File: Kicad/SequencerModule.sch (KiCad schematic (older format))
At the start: 13 parts, among them U1 L78L05_SOT89, U2 MCP4822, U4 TL072

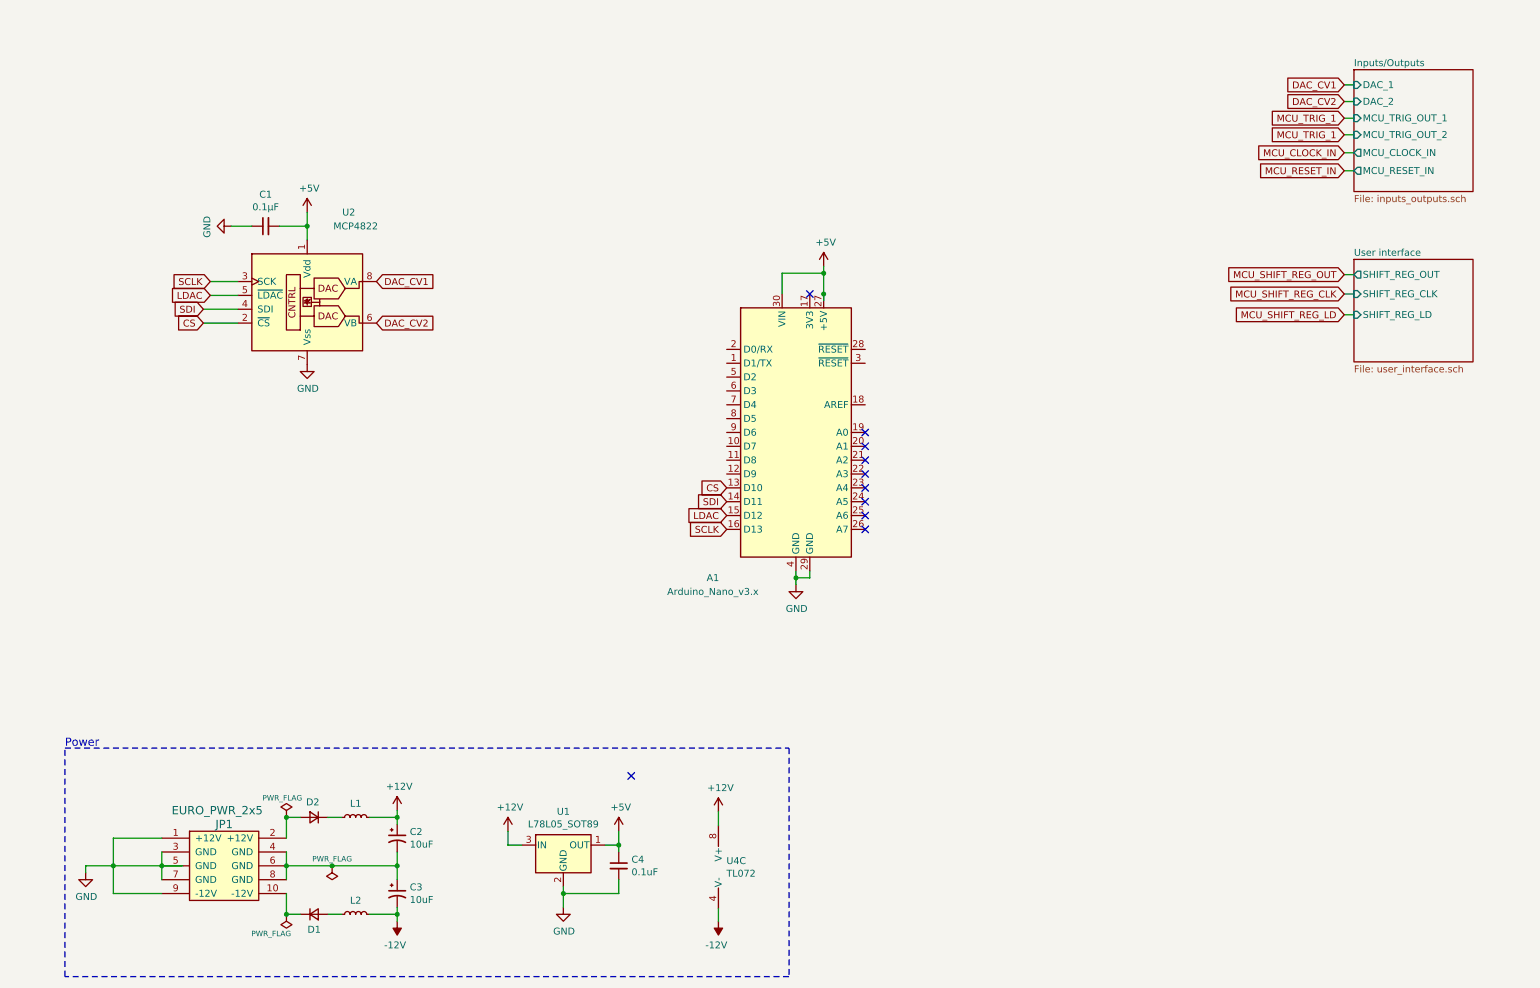
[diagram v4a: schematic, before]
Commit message: correcting some connections
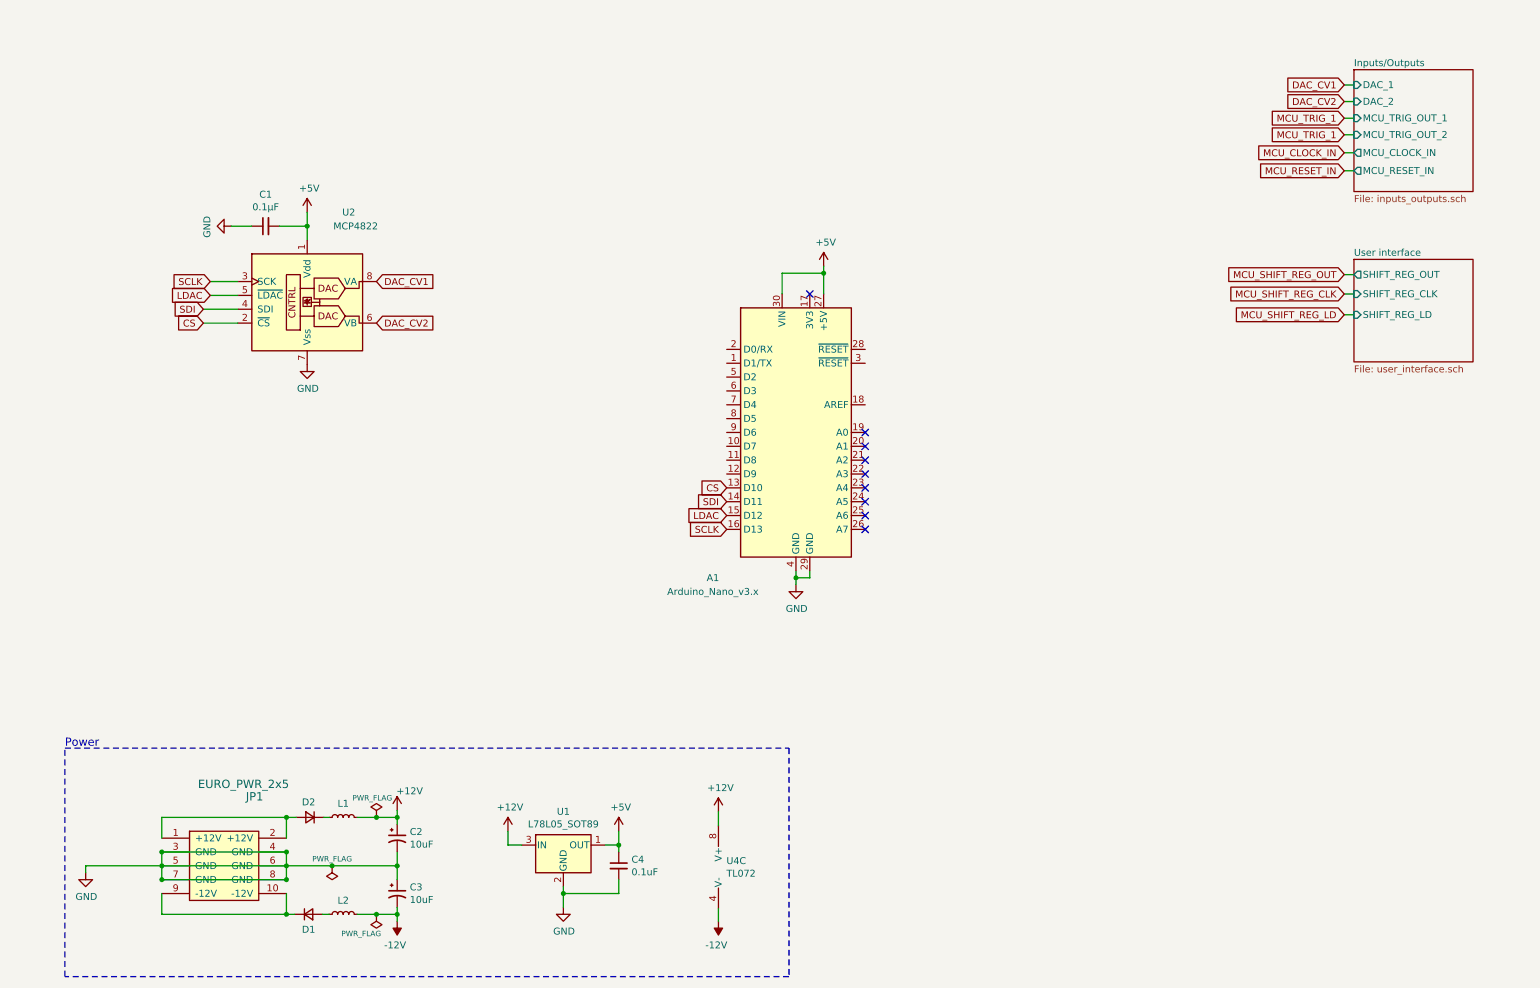
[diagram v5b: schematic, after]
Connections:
- wire segments 65 -> 67
- no-connect marks 10 -> 9
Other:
- moved on the sheet: D1, D2, L1, L2
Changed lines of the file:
@@
 L Device:D_Small D2
 U 1 1 5FB17EBE
-P 2650 6400
-F 0 "D2" H 2660 6290 50  0000 C CNN
-F 1 "D_Small" H 2650 6284 50  0001 C CNN
-F 2 "" V 2650 6400 50  0001 C CNN
-F 3 "~" V 2650 6400 50  0001 C CNN
-	1    2650 6400
+P 2620 6400
+F 0 "D2" H 2630 6290 50  0000 C CNN
+F 1 "D_Small" H 2620 6284 50  0001 C CNN
+F 2 "" V 2620 6400 50  0001 C CNN
+F 3 "~" V 2620 6400 50  0001 C CNN
+	1    2620 6400
 	-1   0    0    1
 $EndComp
@@
 L Device:D_Small D1
 U 1 1 5FB182A9
-P 2650 7100
-F 0 "D1" H 2650 6990 50  0000 C CNN
-F 1 "D_Small" H 2650 6850 50  0001 C CNN
-F 2 "" V 2650 7100 50  0001 C CNN
-F 3 "~" V 2650 7100 50  0001 C CNN
-	1    2650 7100
+P 2610 7100
+F 0 "D1" H 2610 6990 50  0000 C CNN
+F 1 "D_Small" H 2610 6850 50  0001 C CNN
+F 2 "" V 2610 7100 50  0001 C CNN
+F 3 "~" V 2610 7100 50  0001 C CNN
+	1    2610 7100
 	1    0    0    -1
 $EndComp
@@
 L Device:L_Small L1
 U 1 1 5FB1A055
-P 2950 6400
-F 0 "L1" V 3050 6400 50  0000 C CNN
-F 1 "L_Small" V 3044 6400 50  0001 C CNN
-F 2 "" H 2950 6400 50  0001 C CNN
-F 3 "~" H 2950 6400 50  0001 C CNN
-	1    2950 6400
+P 2860 6400
+F 0 "L1" V 2960 6400 50  0000 C CNN
+F 1 "L_Small" V 2954 6400 50  0001 C CNN
+F 2 "" H 2860 6400 50  0001 C CNN
+F 3 "~" H 2860 6400 50  0001 C CNN
+	1    2860 6400
 	0    -1   -1   0
 $EndComp
@@
 L Device:L_Small L2
 U 1 1 5FB1A882
-P 2950 7100
-F 0 "L2" V 3050 7100 50  0000 C CNN
-F 1 "L_Small" V 3044 7100 50  0001 C CNN
-F 2 "" H 2950 7100 50  0001 C CNN
-F 3 "~" H 2950 7100 50  0001 C CNN
-	1    2950 7100
+P 2860 7100
+F 0 "L2" V 2960 7100 50  0000 C CNN
+F 1 "L_Small" V 2954 7100 50  0001 C CNN
+F 2 "" H 2860 7100 50  0001 C CNN
+F 3 "~" H 2860 7100 50  0001 C CNN
+	1    2860 7100
 	0    -1   -1   0
 $EndComp
 Wire Wire Line
-	2750 6400 2850 6400
-Wire Wire Line
-	2750 7100 2850 7100
+	2720 6400 2760 6400
+Wire Wire Line
+	2710 7100 2760 7100
 $Comp
 L power:+12V #PWR0104
@@
 P 3250 6350
 F 0 "#PWR0104" H 3250 6200 50  0001 C CNN
-F 1 "+12V" H 3265 6523 50  0000 C CNN
+F 1 "+12V" H 3340 6490 50  0000 C CNN
 F 2 "" H 3250 6350 50  0001 C CNN
 F 3 "" H 3250 6350 50  0001 C CNN
@@
 $EndComp
 Wire Wire Line
-	3050 6400 3250 6400
+	2960 6400 3100 6400
 Wire Wire Line
 	3250 6400 3250 6350
 Wire Wire Line
-	3050 7100 3250 7100
+	2960 7100 3100 7100
 Wire Wire Line
 	3250 7100 3250 7150
@@
 $EndComp
 Wire Wire Line
-	1200 6550 1550 6550
-Wire Wire Line
 	2450 6550 2450 6400
 Wire Wire Line
-	2450 6400 2550 6400
-Wire Wire Line
-	1200 6950 1550 6950
+	2450 6400 2520 6400
 Wire Wire Line
 	2450 6950 2450 7100
 Wire Wire Line
-	2450 7100 2550 7100
+	2450 7100 2510 7100
 $Comp
 L Device:CP1_Small C3
@@
 Wire Wire Line
 	2450 6850 2450 6750
-Connection ~ 1200 6750
-Wire Wire Line
-	1700 6750 1550 6750
 $Comp
 L power:GND #PWR0106
@@
 Wire Wire Line
 	1000 6800 1000 6750
-Wire Wire Line
-	1000 6750 1200 6750
 $Comp
 L power:+12V #PWR0107
@@
 $EndComp
 Wire Wire Line
-	6330 2670 6330 2620
-Wire Wire Line
 	6330 2420 6330 2470
-Connection ~ 6330 2620
 Wire Wire Line
 	6030 2620 6030 2470
 Wire Wire Line
 	6030 2470 6330 2470
-Connection ~ 6330 2470
-Wire Wire Line
-	6330 2470 6330 2620
 Text GLabel 5630 4020 0    50   Input ~ 0
 CS
@@
 U 1 1 5FBBE1F9
 P 2000 6750
-F 0 "JP1" H 2000 7050 60  0000 C CNN
-F 1 "EURO_PWR_2x5" H 1950 7150 60  0000 C CNN
+F 0 "JP1" H 2220 7250 60  0000 C CNN
+F 1 "EURO_PWR_2x5" H 2140 7340 60  0000 C CNN
 F 2 "" H 2000 6750 60  0000 C CNN
 F 3 "" H 2000 6750 60  0000 C CNN
@@
 $EndComp
 Connection ~ 1550 6750
-Wire Wire Line
-	1200 6750 1550 6750
-Wire Wire Line
-	1200 6550 1200 6750
-Wire Wire Line
-	1200 6750 1200 6950
 Wire Wire Line
 	1550 6650 1550 6750
@@
 Text GLabel 1900 2630 0    50   Input ~ 0
 LDAC
-NoConn ~ 4940 6100
 Text GLabel 5630 4220 0    50   Input ~ 0
 LDAC
@@
 L power:PWR_FLAG #FLG0101
 U 1 1 5FE27D66
-P 2450 6400
-F 0 "#FLG0101" H 2450 6475 50  0001 C CNN
-F 1 "PWR_FLAG" H 2420 6540 39  0000 C CNN
-F 2 "" H 2450 6400 50  0001 C CNN
-F 3 "~" H 2450 6400 50  0001 C CNN
-	1    2450 6400
-	1    0    0    -1
-$EndComp
-Connection ~ 2450 6400
+P 3100 6400
+F 0 "#FLG0101" H 3100 6475 50  0001 C CNN
+F 1 "PWR_FLAG" H 3070 6540 39  0000 C CNN
+F 2 "" H 3100 6400 50  0001 C CNN
+F 3 "~" H 3100 6400 50  0001 C CNN
+	1    3100 6400
+	1    0    0    -1
+$EndComp
 $Comp
 L power:PWR_FLAG #FLG0102
 U 1 1 5FE2804E
-P 2450 7100
-F 0 "#FLG0102" H 2450 7175 50  0001 C CNN
-F 1 "PWR_FLAG" H 2560 7240 39  0000 C CNN
-F 2 "" H 2450 7100 50  0001 C CNN
-F 3 "~" H 2450 7100 50  0001 C CNN
-	1    2450 7100
+P 3100 7100
+F 0 "#FLG0102" H 3100 7175 50  0001 C CNN
+F 1 "PWR_FLAG" H 3210 7240 39  0000 C CNN
+F 2 "" H 3100 7100 50  0001 C CNN
+F 3 "~" H 3100 7100 50  0001 C CNN
+	1    3100 7100
 	-1   0    0    1
 $EndComp
@@
 Wire Wire Line
 	2780 6750 3250 6750
+Wire Wire Line
+	1000 6750 1550 6750
+Wire Wire Line
+	1550 6850 2450 6850
+Connection ~ 1550 6850
+Connection ~ 2450 6850
+Wire Wire Line
+	1550 6650 2450 6650
+Connection ~ 1550 6650
+Connection ~ 2450 6650
+Wire Wire Line
+	1550 6950 1550 7100
+Wire Wire Line
+	1550 7100 2450 7100
+Wire Wire Line
+	1550 6550 1550 6400
+Wire Wire Line
+	1550 6750 2450 6750
+Connection ~ 3100 6400
+Wire Wire Line
+	3100 6400 3250 6400
+Connection ~ 3100 7100
+Wire Wire Line
+	3100 7100 3250 7100
+Wire Wire Line
+	1550 6400 2450 6400
+Connection ~ 2450 6400
+Wire Wire Line
+	6330 2620 6330 2470
+Connection ~ 6330 2470
 $EndSCHEMATC
